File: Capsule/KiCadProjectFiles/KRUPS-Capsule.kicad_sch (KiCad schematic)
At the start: 116 parts, among them J1 JST_GH_BM04B, J11 BM04B-JST-GH, J12 Micro_SD_Card_Det2, J2 JST_VH_B4P-VH-B, J3 JST_GH_BM04B, J5 JST_VH_B2P, J7 Conn_01x04, J8 JST_GH_BM04B-GHS, Q1 2N7002K, U1 UM3232EEAE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

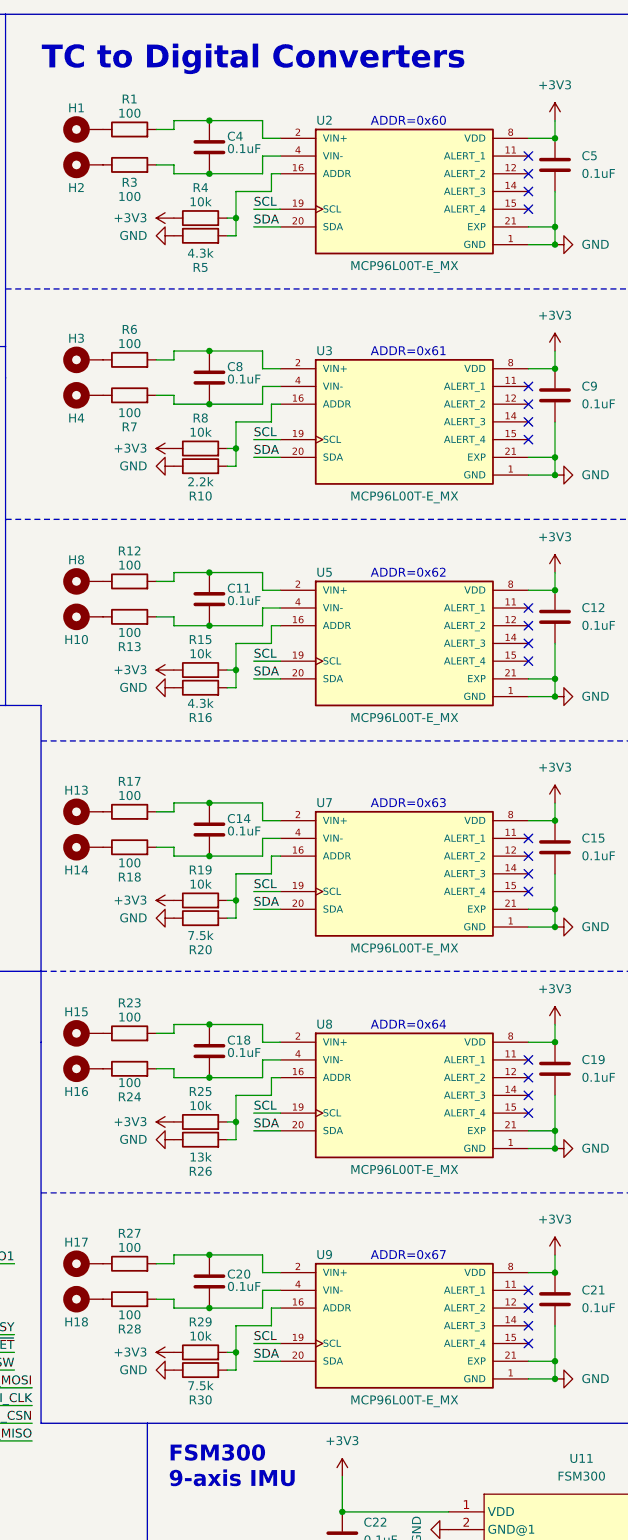
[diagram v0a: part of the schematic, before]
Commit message: updated capsule schematic with improvised thermocouple changes. created schematic pdf
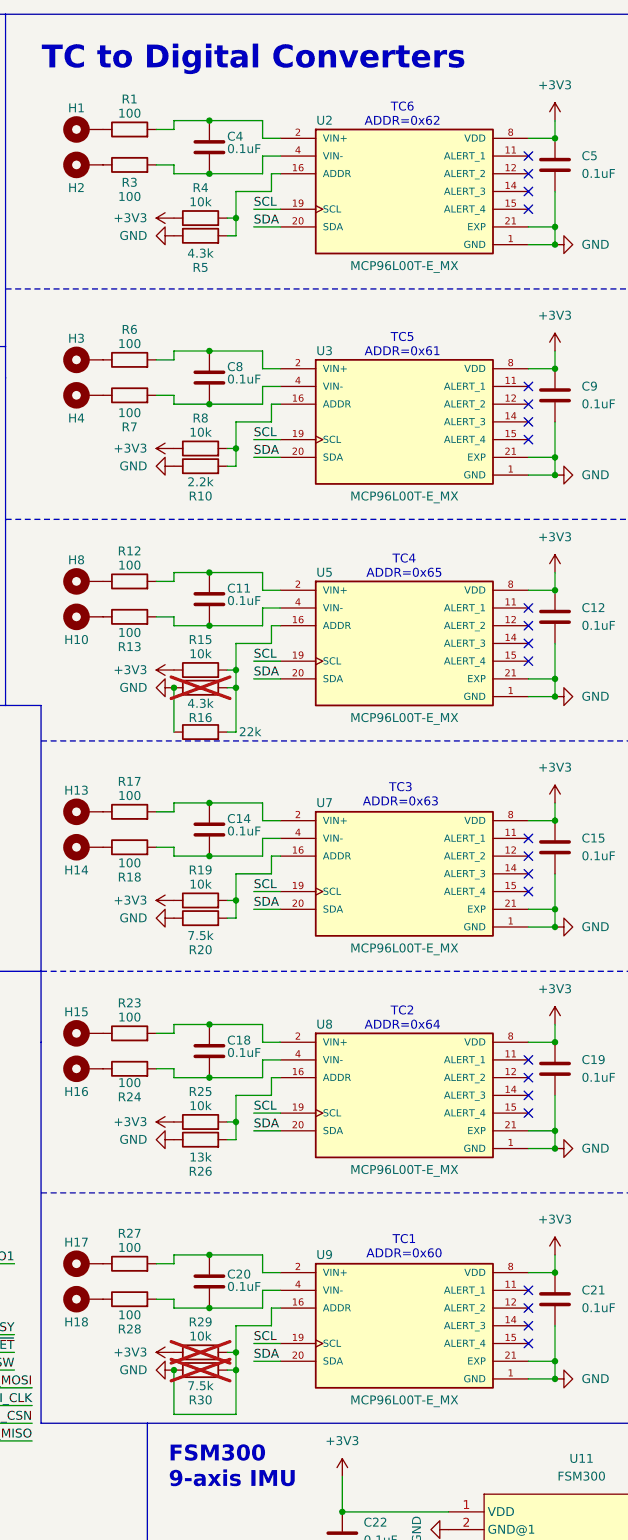
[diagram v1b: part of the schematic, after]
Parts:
- added R31: 22k, symbol Device:R
- R16, R29, R30: now not fitted
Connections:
- net EXP__1: now also R29.2, R30.2, U9.16 (ADDR), R31.1
- net at R15.2, R16.2, U5.16 (ADDR): now also R31.2
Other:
- note added: "TC1 ADDR=0x60"
- note added: "TC2 ADDR=0x64"
- note added: "TC3 ADDR=0x63"
- note added: "TC4 ADDR=0x65"
- note added: "TC5 ADDR=0x61"
- note added: "TC6 ADDR=0x62"
- note removed: "ADDR=0x60"
- note removed: "ADDR=0x61"
- note removed: "ADDR=0x62"
- note removed: "ADDR=0x63"
- note removed: "ADDR=0x64"
- note removed: "ADDR=0x67"
- title: KRUPS Flight Computer -> KRUPS Flight Computer - RockSat XG
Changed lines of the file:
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@@
 	(paper "A3")
 	(title_block
-		(title "KRUPS Flight Computer")
-		(date "2025-02-20")
+		(title "KRUPS Flight Computer - RockSat XG")
+		(date "2025-04-20")
 	)
 	(text "Indicator\nLEDs"
@@
 		)
 	)
-	(text "ADDR=0x67"
+	(text "TC1\nADDR=0x60"
 		(exclude_from_sim no)
-		(at 331.724 190.754 0)
+		(at 336.55 189.484 0)
 		(effects
 			(font
 				(size 1.27 1.27)
 			)
-			(justify left)
 		)
 	)
@@
 		)
 	)
-	(text "ADDR=0x63"
+	(text "TC3\nADDR=0x63"
 		(exclude_from_sim no)
-		(at 331.724 125.984 0)
+		(at 336.042 124.714 0)
 		(effects
 			(font
 				(size 1.27 1.27)
 			)
-			(justify left)
 		)
 	)
@@
 		)
 	)
-	(text "ADDR=0x62"
+	(text "TC4\nADDR=0x65"
 		(exclude_from_sim no)
-		(at 331.724 92.964 0)
+		(at 336.55 91.948 0)
 		(effects
 			(font
 				(size 1.27 1.27)
 			)
-			(justify left)
 		)
 	)
@@
 		)
 	)
-	(text "ADDR=0x64"
+	(text "TC2\nADDR=0x64"
 		(exclude_from_sim no)
-		(at 331.724 157.734 0)
+		(at 336.296 156.718 0)
 		(effects
 			(font
 				(size 1.27 1.27)
 			)
-			(justify left)
 		)
 	)
@@
 		)
 	)
-	(text "ADDR=0x61"
+	(text "TC5\nADDR=0x61"
 		(exclude_from_sim no)
-		(at 331.724 61.214 0)
+		(at 336.296 60.198 0)
 		(effects
 			(font
 				(size 1.27 1.27)
 			)
-			(justify left)
 		)
 	)
@@
 		)
 	)
-	(text "ADDR=0x60"
+	(text "TC6\nADDR=0x62"
 		(exclude_from_sim no)
-		(at 331.724 28.194 0)
+		(at 336.296 27.178 0)
 		(effects
 			(font
 				(size 1.27 1.27)
 			)
-			(justify left)
 		)
 	)
@@
 	)
 	(junction
+		(at 303.53 207.01)
+		(diameter 0)
+		(color 0 0 0 0)
+	)
+	(junction
 		(at 358.14 140.97)
 		(diameter 0)
@@
 	)
 	(junction
+		(at 303.53 109.22)
+		(diameter 0)
+		(color 0 0 0 0)
+	)
+	(junction
 		(at 229.87 69.85)
 		(diameter 0)
@@
 	)
 	(junction
+		(at 312.42 109.22)
+		(diameter 0)
+		(color 0 0 0 0)
+	)
+	(junction
 		(at 166.37 140.97)
 		(diameter 0)
@@
 	)
 	(junction
+		(at 312.42 207.01)
+		(diameter 0)
+		(color 0 0 0 0)
+	)
+	(junction
 		(at 358.14 128.27)
 		(diameter 0)
@@
 	(wire
 		(pts
+			(xy 303.53 207.01) (xy 303.53 213.36)
+		)
+		(stroke
+			(width 0)
+			(type default)
+		)
+	)
+	(wire
+		(pts
 			(xy 317.5 200.66) (xy 317.5 198.12)
 		)
@@
 	(wire
 		(pts
+			(xy 312.42 115.57) (xy 311.15 115.57)
+		)
+		(stroke
+			(width 0)
+			(type default)
+		)
+	)
+	(wire
+		(pts
 			(xy 311.15 74.93) (xy 312.42 74.93)
 		)
@@
 	(wire
 		(pts
+			(xy 312.42 109.22) (xy 312.42 115.57)
+		)
+		(stroke
+			(width 0)
+			(type default)
+		)
+	)
+	(wire
+		(pts
 			(xy 358.14 190.5) (xy 358.14 193.04)
 		)
@@
 	(wire
 		(pts
+			(xy 303.53 213.36) (xy 312.42 213.36)
+		)
+		(stroke
+			(width 0)
+			(type default)
+		)
+	)
+	(wire
+		(pts
 			(xy 312.42 173.99) (xy 312.42 171.45)
 		)
@@
 	(wire
 		(pts
+			(xy 303.53 109.22) (xy 303.53 115.57)
+		)
+		(stroke
+			(width 0)
+			(type default)
+		)
+	)
+	(wire
+		(pts
 			(xy 247.65 21.59) (xy 246.38 21.59)
 		)
@@
 	(wire
 		(pts
+			(xy 312.42 213.36) (xy 312.42 207.01)
+		)
+		(stroke
+			(width 0)
+			(type default)
+		)
+	)
+	(wire
+		(pts
 			(xy 100.33 186.69) (xy 113.03 186.69)
 		)
@@
 		(in_bom yes)
 		(on_board yes)
-		(dnp no)
+		(dnp yes)
 		(property "Reference" "R16"
 			(at 307.34 113.538 90)
@@
 		(in_bom yes)
 		(on_board yes)
-		(dnp no)
+		(dnp yes)
 		(property "Reference" "R29"
 			(at 307.34 200.152 90)
@@
 		(in_bom yes)
 		(on_board yes)
-		(dnp no)
+		(dnp yes)
 		(property "Reference" "R30"
 			(at 307.34 211.328 90)
@@
 					(unit 1)
 				)
+			)
+		)
+	)
+	(symbol
+		(lib_id "Device:R")
+		(at 307.34 115.57 90)
+		(unit 1)
+		(exclude_from_sim no)
+		(in_bom yes)
+		(on_board yes)
+		(dnp no)
+		(property "Reference" "R31"
+			(at 307.34 109.22 90)
+			(effects
+				(font
+					(size 1.27 1.27)
+				)
+				(hide yes)
+			)
+		)
+		(property "Value" "22k"
+			(at 314.452 115.57 90)
+			(effects
+				(font
+					(size 1.27 1.27)
+				)
+			)
+		)
+		(property "Footprint" ""
+			(at 307.34 117.348 90)
+			(effects
+				(font
+					(size 1.27 1.27)
+				)
+				(hide yes)
+			)
+		)
+		(property "Datasheet" "~"
+			(at 307.34 115.57 0)
+			(effects
+				(font
+					(size 1.27 1.27)
+				)
+				(hide yes)
+			)
+		)
+		(property "Description" "Resistor"
+			(at 307.34 115.57 0)
+			(effects
+				(font
+					(size 1.27 1.27)
+				)
+				(hide yes)
+			)
+		)
+		(pin "2"
+		)
+		(pin "1"
+		)
+		(instances
+			(project ""
+				(path "/6241326a-b012-42a4-9d28-e009e6f6a957"
+					(reference "R31")
+					(unit 1)
+				)
